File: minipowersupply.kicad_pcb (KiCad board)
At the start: 2 copper layers, 145.9 x 37.4 mm, 56 parts, among them J1 Conn_01x08_Female, J2 Conn_01x08_Female, J3 Conn_01x03_Female, J4 Conn_01x08_Female, J5 Conn_01x03_Female, J6 Conn_01x03_Female, J7 Conn_01x02_Female, J8 Conn_01x08_Female, J9 Conn_01x02_Female, Q1 BC817, U1 LM7805_TO220, U10 LM317L_TO92, U11 LM337L_TO92, U14 ACS70331EOLCTR-2P5U3, U2 ACS70331EOLCTR-2P5U3, U3 ACS70331EOLCTR-2P5U3, U4 ACS70331EOLCTR-2P5U3, U5 ACS70331EOLCTR-2P5U3, U9 CD74HC4067SM

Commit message: last TH mounting board
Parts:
- removed the R10 at (148.8, 70.3)
- removed R22, R23: R_Small, Resistor_THT:R_Axial_DIN0207_L6.3mm_D2.5mm_P5.08mm_Vertical
- removed the R9 at (92.0, 113.2)
- removed U14: ACS70331EOLCTR-2P5U3, ACS70331EOLCTR-2P5U3:SOIC127P600X175-8N
- added C39: C, Capacitor_THT:C_Disc_D8.0mm_W5.0mm_P5.00mm, F.Cu at (41.4, 107.2)
- added D7: DIODE, Diode_THT:D_T-1_P10.16mm_Horizontal, F.Cu at (158.6, 43.3)
- added D8: DIODE, Diode_THT:D_T-1_P10.16mm_Horizontal, F.Cu at (148.5, 40.1)
- added D9: DIODE, Diode_THT:D_T-1_P10.16mm_Horizontal, F.Cu at (59.8, 137.4)
- added J1: Conn_01x01_Female, Connector_PinHeader_2.54mm:PinHeader_1x01_P2.54mm_Vertical, F.Cu at (99.3, 116.3)
- added J2: Conn_01x03_Male, Connector_PinHeader_2.54mm:PinHeader_1x03_P2.54mm_Horizontal, F.Cu at (106.5, 92.5)
- added J3: Conn_01x01_Female, Connector_PinHeader_2.54mm:PinHeader_1x01_P2.54mm_Vertical, F.Cu at (107.7, 116.3)
- added J4: Conn_01x01_Female, Connector_PinHeader_2.54mm:PinHeader_1x01_P2.54mm_Vertical, F.Cu at (136.1, 116.3)
- added J5: Conn_01x03_Male, Connector_PinHeader_2.54mm:PinHeader_1x03_P2.54mm_Horizontal, B.Cu at (131.3, 92.5)
- added J6: Conn_01x01_Female, Connector_PinHeader_2.54mm:PinHeader_1x01_P2.54mm_Vertical, F.Cu at (125.0, 116.3)
- added J7: Conn_01x01_Female, Connector_PinHeader_2.54mm:PinHeader_1x01_P2.54mm_Vertical, F.Cu at (118.4, 116.3)
- added J8: Conn_01x03_Male, Connector_PinHeader_2.54mm:PinHeader_1x03_P2.54mm_Horizontal, B.Cu at (121.4, 92.5)
- added J9: Conn_01x01_Female, Connector_PinHeader_2.54mm:PinHeader_1x01_P2.54mm_Vertical, F.Cu at (112.8, 116.3)
- added R1: R_Small, Resistor_THT:R_Axial_DIN0207_L6.3mm_D2.5mm_P5.08mm_Vertical, F.Cu at (105.9, 107.4)
- added R14: R, Resistor_THT:R_Axial_DIN0207_L6.3mm_D2.5mm_P5.08mm_Vertical, F.Cu at (91.3, 104.4)
- added R15: R, Resistor_THT:R_Axial_DIN0207_L6.3mm_D2.5mm_P5.08mm_Vertical, F.Cu at (86.6, 101.2)
- added R16: R_Small, Resistor_THT:R_Axial_DIN0207_L6.3mm_D2.5mm_P5.08mm_Vertical, F.Cu at (97.3, 107.4)
- added R17: R_Small, Resistor_THT:R_Axial_DIN0207_L6.3mm_D2.5mm_P5.08mm_Vertical, F.Cu at (102.0, 110.6)
- added R18: R, Resistor_THT:R_Axial_DIN0207_L6.3mm_D2.5mm_P5.08mm_Vertical, F.Cu at (76.8, 137.0)
- added R19: R, Resistor_THT:R_Axial_DIN0207_L6.3mm_D2.5mm_P5.08mm_Vertical, F.Cu at (86.4, 120.8)
- added R2: R_Small, Resistor_THT:R_Axial_DIN0207_L6.3mm_D2.5mm_P5.08mm_Vertical, F.Cu at (110.5, 110.7)
- added R20: R, Resistor_THT:R_Axial_DIN0207_L6.3mm_D2.5mm_P5.08mm_Vertical, F.Cu at (86.4, 116.8)
- added U1: ACS70331EOLCTR-2P5U3, ACS70331EOLCTR-2P5U3:SOIC127P600X175-8N, F.Cu at (107.5, 101.8)
- added U10: ACS70331EOLCTR-2P5U3, ACS70331EOLCTR-2P5U3:SOIC127P600X175-8N, F.Cu at (99.1, 101.8)
- Q1: moved to F.Cu
- R11: value R_Small -> 698
- R3: value 698 -> R_Small
- U4: value ACS70331EOLCTR-2P5U3 -> CD74HC4067SM; footprint ACS70331EOLCTR-2P5U3:SOIC127P600X175-8N -> Package_SO:SSOP-24_5.3x8.2mm_P0.65mm
- U6: renamed from U1; moved to B.Cu
- U9: value CD74HC4067SM -> Opamp_Dual; footprint Package_SO:SSOP-24_5.3x8.2mm_P0.65mm -> Package_TO_SOT_SMD:SOT-223-8
- moved R3 115.2 mm to (132.1, 107.4)
- moved C27 70.1 mm to (139.8, 50.8)
- moved R10 67.6 mm to (148.8, 47.4), turned to -90 degrees
- moved C29 65.9 mm to (157.5, 50.8), turned to 180 degrees
- moved U5 49.7 mm to (118.2, 102.1), turned to 180 degrees
- moved R4 48.2 mm to (136.7, 110.6), turned to 180 degrees
- moved U9 48.0 mm to (88.7, 111.2), turned to 180 degrees
- moved R5 43.8 mm to (123.7, 107.4)
- moved U2 43.0 mm to (134.7, 102.1), turned to 180 degrees
- moved U7 39.9 mm to (166.9, 43.1), turned to -90 degrees
- moved A1 39.8 mm to (60.0, 92.7)
- moved J17 37.9 mm to (168.0, 54.5)
- moved R8 37.7 mm to (119.7, 110.6), turned to 180 degrees
- moved J12 37.4 mm to (119.5, 59.6)
- moved J14 37.1 mm to (124.3, 59.6)
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- renumbered C1 to C23, C2 to C24, C3 to C27, C4 to C28, C5 to C29, C6 to C30, C7 to C31, C8 to C32, C9 to C33, J3 to J10, J1 to J11, J5 to J12, J2 to J13, J6 to J14, J4 to J15, J7 to J16, J8 to J17, J9 to J18, R2 to R10, R16 to R12, R17 to R13, R1 to R9, U10 to U7, U11 to U8
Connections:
- net Earth renamed /Unregulated Power/GND
- A1 pad 20: Net-(A1-Pad20) -> unconnected-(A1-Pad20)
- A1 pad 29: GNDREF -> / Measure and Mux/GND
- A1 pad 4: GNDREF -> / Measure and Mux/GND
- DS1 pad 1: unconnected-(DS1-Pad1) -> / Measure and Mux/GND
- DS1 pad 30: unconnected-(DS1-Pad1) -> / Measure and Mux/GND
- R11 pad 1: / Measure and Mux/Curent and Volt8/Vsense -> Net-(D7-Pad2)
- R11 pad 2: / Measure and Mux/Curent and Volt4/GND -> /Clock and TTL/GND_0
- R3 pad 1: Net-(D7-Pad2) -> / Measure and Mux/Curent and Volt6/Out V
- R3 pad 2: /Clock and TTL/GND_0 -> / Measure and Mux/Curent and Volt6/Vsense
- R4 pad 1: / Measure and Mux/Curent and Volt5/Out V -> / Measure and Mux/Curent and Volt6/Vsense
- R4 pad 2: / Measure and Mux/Curent and Volt5/Vsense -> / Measure and Mux/GND
- R5 pad 1: / Measure and Mux/Curent and Volt5/Vsense -> / Measure and Mux/Curent and Volt7/Out V
- R5 pad 2: / Measure and Mux/Curent and Volt4/GND -> / Measure and Mux/Curent and Volt7/Vsense
- R6 pad 1: / Measure and Mux/Curent and Volt6/Out V -> / Measure and Mux/Curent and Volt7/Vsense
- R6 pad 2: / Measure and Mux/Curent and Volt6/Vsense -> / Measure and Mux/GND
- R7 pad 1: / Measure and Mux/Curent and Volt6/Vsense -> / Measure and Mux/Curent and Volt8/Out V
- R7 pad 2: / Measure and Mux/Curent and Volt4/GND -> / Measure and Mux/Curent and Volt8/Vsense
- R8 pad 1: / Measure and Mux/Curent and Volt7/Out V -> / Measure and Mux/Curent and Volt8/Vsense
- R8 pad 2: / Measure and Mux/Curent and Volt7/Vsense -> / Measure and Mux/GND
- U2 pad 1: / Measure and Mux/Curent and Volt5/Out V -> / Measure and Mux/Curent and Volt6/Out V
- U2 pad 2: / Measure and Mux/Curent and Volt5/Out V -> / Measure and Mux/Curent and Volt6/Out V
- U2 pad 3: / Measure and Mux/Vunreg- -> / Measure and Mux/Curent and Volt6/Vin
- U2 pad 4: / Measure and Mux/Vunreg- -> / Measure and Mux/Curent and Volt6/Vin
- U2 pad 5: / Measure and Mux/Curent and Volt4/GND -> / Measure and Mux/GND
- U2 pad 7: / Measure and Mux/Curent and Volt5/Isense -> / Measure and Mux/Curent and Volt6/Isense
- U3 pad 1: / Measure and Mux/Curent and Volt6/Out V -> / Measure and Mux/Curent and Volt7/Out V
- U3 pad 2: / Measure and Mux/Curent and Volt6/Out V -> / Measure and Mux/Curent and Volt7/Out V
- U3 pad 3: / Measure and Mux/Curent and Volt6/Vin -> / Measure and Mux/Curent and Volt7/Vin
- U3 pad 4: / Measure and Mux/Curent and Volt6/Vin -> / Measure and Mux/Curent and Volt7/Vin
- U3 pad 5: / Measure and Mux/Curent and Volt4/GND -> / Measure and Mux/GND
- U3 pad 7: / Measure and Mux/Curent and Volt6/Isense -> / Measure and Mux/Curent and Volt7/Isense
- U4 pad 1: / Measure and Mux/Curent and Volt7/Out V -> / Measure and Mux/Aout
- U4 pad 2: / Measure and Mux/Curent and Volt7/Out V -> / Measure and Mux/Curent and Volt7/Isense
- U4 pad 3: / Measure and Mux/Curent and Volt7/Vin -> / Measure and Mux/Unity Inverter1/Ainv
- U4 pad 4: / Measure and Mux/Curent and Volt7/Vin -> / Measure and Mux/Curent and Volt6/Isense
- U4 pad 5: / Measure and Mux/Curent and Volt4/GND -> / Measure and Mux/Curent and Volt6/Vsense
- U4 pad 6: unconnected-(U4-Pad6) -> / Measure and Mux/Curent and Volt5/Isense
- U4 pad 7: / Measure and Mux/Curent and Volt7/Isense -> / Measure and Mux/Unity Inverter/Ainv
- U4 pad 8: / Measure and Mux/3v3 -> / Measure and Mux/Curent and Volt4/Isense
- U5 pad 5: / Measure and Mux/Curent and Volt4/GND -> / Measure and Mux/GND
- U9 pad 1: / Measure and Mux/Aout -> / Measure and Mux/Unity Inverter/Ainv
- U9 pad 2: / Measure and Mux/Curent and Volt7/Isense -> / Measure and Mux/Curent and Volt5/Vsense
- U9 pad 3: / Measure and Mux/Curent and Volt7/Vsense -> Net-(R19-Pad1)
- U9 pad 4: / Measure and Mux/Curent and Volt6/Isense -> / Measure and Mux/Vunreg-
- U9 pad 5: / Measure and Mux/Curent and Volt6/Vsense -> Net-(R14-Pad1)
- U9 pad 6: / Measure and Mux/Curent and Volt5/Isense -> / Measure and Mux/Curent and Volt7/Vsense
- U9 pad 7: / Measure and Mux/Curent and Volt5/Vsense -> / Measure and Mux/Unity Inverter1/Ainv
- U9 pad 8: / Measure and Mux/Curent and Volt4/Isense -> / Measure and Mux/Vunreg+
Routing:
- net (no net): track 36.7 -> 0.00 mm
- net Net-(J16-Pad2): track 0.00 -> 17.5 mm
- net /Clock and TTL/CK: track 42.1 -> 25.6 mm, vias 1 -> 0
- net Net-(C32-Pad1): track 8.62 -> 24.9 mm
- net /Unregulated Power/V-: track 40.5 -> 49.3 mm
- net Net-(J18-Pad2): track 0.00 -> 7.56 mm
- net Net-(C33-Pad2): track 23.3 -> 30.6 mm
- net /Unregulated Power/V+: track 69.1 -> 62.2 mm
- net Net-(C31-Pad1): track 27.8 -> 34.1 mm
- net Net-(C25-Pad2): track 12.2 -> 18.2 mm
- net Net-(C22-Pad1): track 12.7 -> 18.7 mm
- net Net-(C26-Pad1): track 7.46 -> 13.4 mm
- net Net-(J11-Pad8): track 7.29 -> 12.9 mm
- net /Clock and TTL/GND_0: track 0.00 -> 3.80 mm, vias 0 -> 1
- net Net-(C27-Pad1): track 11.7 -> 9.09 mm
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- added copper zone on B.Cu, net /DualAdj/GND
- added copper zone on F.Cu, net /DualAdj/GND
- removed copper zone on B.Cu, net (none)
- removed copper zone on F.Cu, net (none)
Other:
- board size 145.9 x 37.4 mm -> 149.9 x 37.3 mm

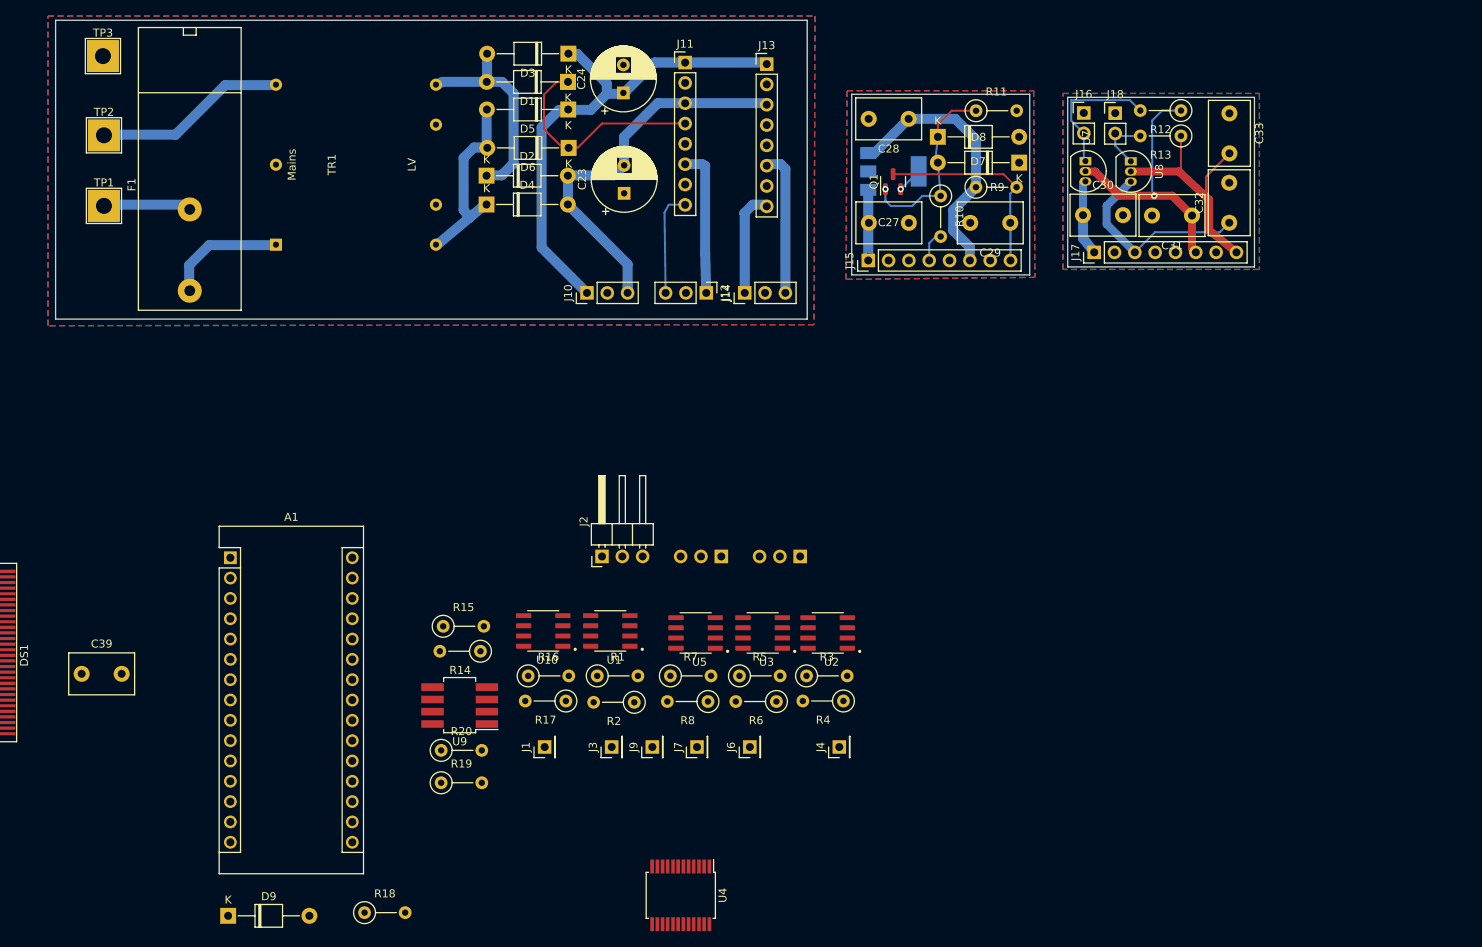
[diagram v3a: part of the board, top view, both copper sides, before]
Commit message: all SMD components going into boards
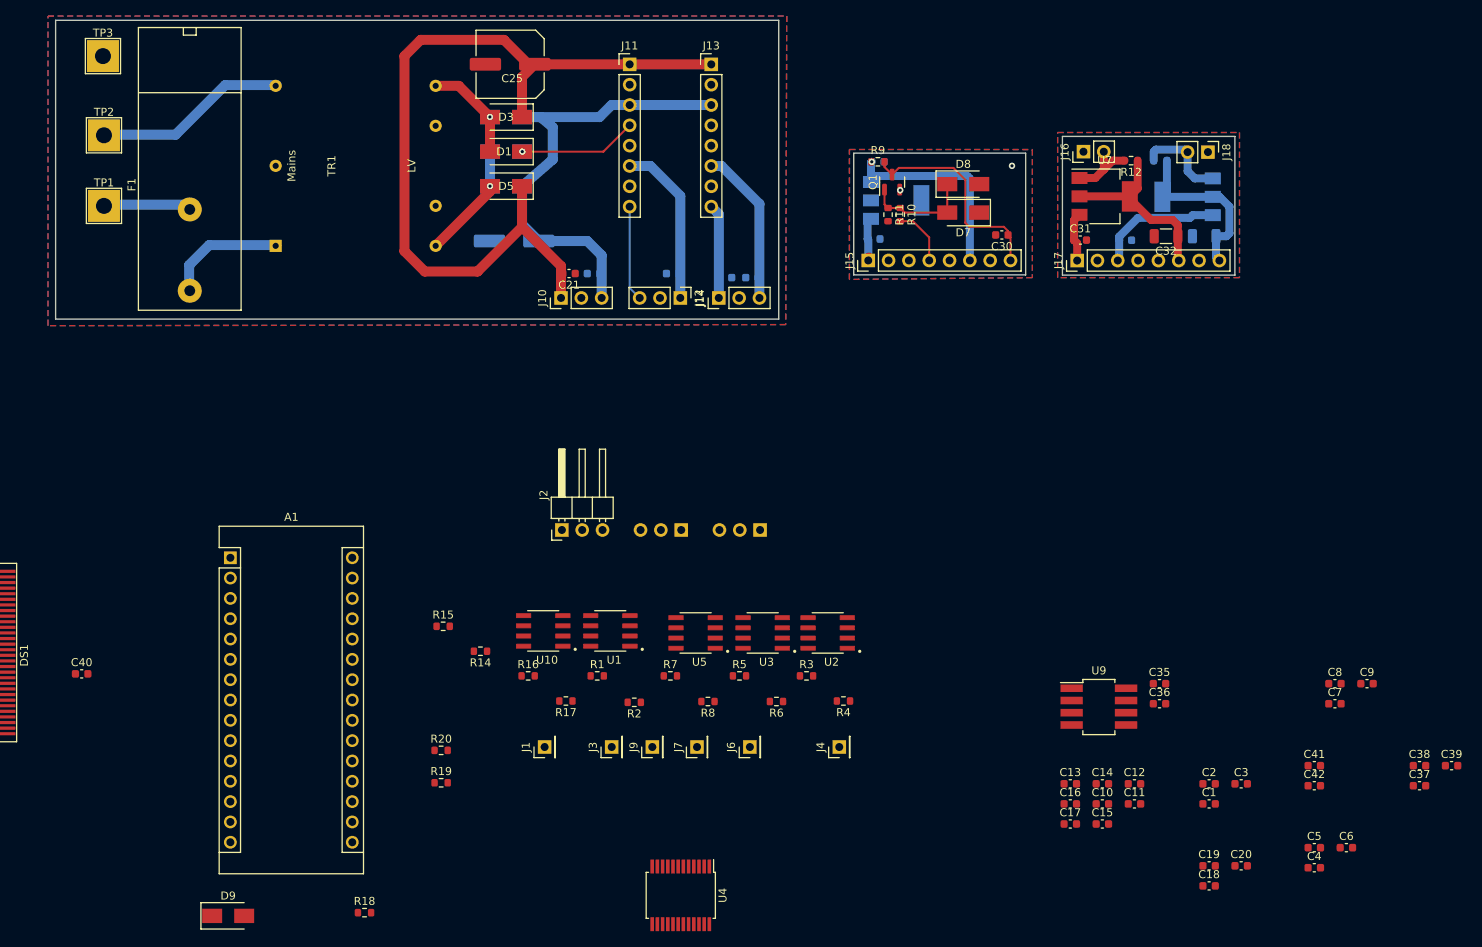
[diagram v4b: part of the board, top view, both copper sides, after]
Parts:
- added C1: 0.1uF, Capacitor_SMD:C_0603_1608Metric, F.Cu at (182.4, 123.4)
- added C10: 0.1uF, Capacitor_SMD:C_0603_1608Metric, F.Cu at (169.0, 123.4)
- added C11: 0.1uF, Capacitor_SMD:C_0603_1608Metric, F.Cu at (173.0, 123.4)
- added C12: 0.1uF, Capacitor_SMD:C_0603_1608Metric, F.Cu at (173.0, 120.9)
- added C13: 0.1uF, Capacitor_SMD:C_0603_1608Metric, F.Cu at (165.0, 120.9)
- added C14: 0.1uF, Capacitor_SMD:C_0603_1608Metric, F.Cu at (169.0, 120.9)
- added C15: 0.1uF, Capacitor_SMD:C_0603_1608Metric, F.Cu at (169.0, 126.0)
- added C16: 0.1uF, Capacitor_SMD:C_0603_1608Metric, F.Cu at (165.0, 123.4)
- added C17: 0.1uF, Capacitor_SMD:C_0603_1608Metric, F.Cu at (165.0, 126.0)
- added C18: 0.1uF, Capacitor_SMD:C_0603_1608Metric, F.Cu at (182.4, 133.7)
- added C19: 0.1uF, Capacitor_SMD:C_0603_1608Metric, F.Cu at (182.4, 131.2)
- added C2: 0.1uF, Capacitor_SMD:C_0603_1608Metric, F.Cu at (182.4, 120.9)
- added C20: 0.1uF, Capacitor_SMD:C_0603_1608Metric, F.Cu at (186.4, 131.2)
- added C21: 0.1uF, Capacitor_SMD:C_0603_1608Metric, F.Cu at (102.4, 57.1)
- added C22: 0.1uF, Capacitor_SMD:C_0603_1608Metric, B.Cu at (105.4, 57.1)
- added C23: 0.1uF, Capacitor_SMD:C_0603_1608Metric, B.Cu at (115.3, 57.1)
- added C26: 0.1uF, Capacitor_SMD:C_0603_1608Metric, B.Cu at (125.2, 57.7)
- added C27: 0.1uF, Capacitor_SMD:C_0603_1608Metric, B.Cu at (121.9, 57.7)
- added C3: 0.1uF, Capacitor_SMD:C_0603_1608Metric, F.Cu at (186.4, 120.9)
- added C35: 0.1uF, Capacitor_SMD:C_0603_1608Metric, F.Cu at (176.2, 108.4)
- added C36: 0.1uF, Capacitor_SMD:C_0603_1608Metric, F.Cu at (176.2, 110.9)
- added C37: 0.1uF, Capacitor_SMD:C_0603_1608Metric, F.Cu at (208.7, 121.2)
- added C38: 0.1uF, Capacitor_SMD:C_0603_1608Metric, F.Cu at (208.7, 118.7)
- added C39: 0.1uF, Capacitor_SMD:C_0603_1608Metric, F.Cu at (212.7, 118.7)
- added C4: 0.1uF, Capacitor_SMD:C_0603_1608Metric, F.Cu at (195.5, 131.4)
- added C41: 0.1uF, Capacitor_SMD:C_0603_1608Metric, F.Cu at (195.5, 118.7)
- added C42: 0.1uF, Capacitor_SMD:C_0603_1608Metric, F.Cu at (195.5, 121.2)
- added C5: 0.1uF, Capacitor_SMD:C_0603_1608Metric, F.Cu at (195.5, 128.9)
- added C6: 0.1uF, Capacitor_SMD:C_0603_1608Metric, F.Cu at (199.5, 128.9)
- added C7: 0.1uF, Capacitor_SMD:C_0603_1608Metric, F.Cu at (198.1, 110.9)
- added C8: 0.1uF, Capacitor_SMD:C_0603_1608Metric, F.Cu at (198.1, 108.4)
- added C9: 0.1uF, Capacitor_SMD:C_0603_1608Metric, F.Cu at (202.1, 108.4)
- C24: renamed from C23; footprint Capacitor_THT:CP_Radial_D8.0mm_P3.50mm -> Capacitor_SMD:C_Elec_8x6.2; moved to B.Cu
- C25: renamed from C24; footprint Capacitor_THT:CP_Radial_D8.0mm_P3.50mm -> Capacitor_SMD:C_Elec_8x6.2
- C28: renamed from C27; value 100nF -> 0.1uF; footprint Capacitor_THT:C_Disc_D8.0mm_W5.0mm_P5.00mm -> Capacitor_SMD:C_0603_1608Metric; moved to B.Cu
- C29: renamed from C28; value 100nF -> 0.1uF; footprint Capacitor_THT:C_Disc_D8.0mm_W5.0mm_P5.00mm -> Capacitor_SMD:C_0603_1608Metric; moved to B.Cu
- C30: renamed from C29; value 100nF -> 0.1uF; footprint Capacitor_THT:C_Disc_D8.0mm_W5.0mm_P5.00mm -> Capacitor_SMD:C_0603_1608Metric
- C31: renamed from C30; value 100nF -> 0.1uF; footprint Capacitor_THT:C_Disc_D8.0mm_W5.0mm_P5.00mm -> Capacitor_SMD:C_0603_1608Metric
- C32: renamed from C31; footprint Capacitor_THT:C_Disc_D8.0mm_W5.0mm_P5.00mm -> Capacitor_SMD:C_1206_3216Metric
- C33: renamed from C32; value 100nF -> 0.1uF; footprint Capacitor_THT:C_Disc_D8.0mm_W5.0mm_P5.00mm -> Capacitor_SMD:C_0603_1608Metric; moved to B.Cu
- C34: renamed from C33; footprint Capacitor_THT:C_Disc_D8.0mm_W5.0mm_P5.00mm -> Capacitor_SMD:C_1206_3216Metric; moved to B.Cu
- C40: renamed from C39; value C -> 0.1uF; footprint Capacitor_THT:C_Disc_D8.0mm_W5.0mm_P5.00mm -> Capacitor_SMD:C_0603_1608Metric
- D1, D3, D5: value D -> S1K-13-F; footprint Diode_THT:D_T-1_P10.16mm_Horizontal -> Diode_SMD:D_SMA
- D2, D4, D6: value D -> S1K-13-F; footprint Diode_THT:D_T-1_P10.16mm_Horizontal -> Diode_SMD:D_SMA; moved to B.Cu
- D7, D8, D9: value DIODE -> S1K-13-F; footprint Diode_THT:D_T-1_P10.16mm_Horizontal -> Diode_SMD:D_SMA
- R1, R16, R3, R5, R7: value R_Small -> 20k; footprint Resistor_THT:R_Axial_DIN0207_L6.3mm_D2.5mm_P5.08mm_Vertical -> Resistor_SMD:R_0603_1608Metric
- R10, R11, R12, R9: footprint Resistor_THT:R_Axial_DIN0207_L6.3mm_D2.5mm_P5.08mm_Vertical -> Resistor_SMD:R_0603_1608Metric
- R13: footprint Resistor_THT:R_Axial_DIN0207_L6.3mm_D2.5mm_P5.08mm_Vertical -> Resistor_SMD:R_0603_1608Metric; moved to B.Cu
- R14, R15, R18, R19, R20: value R -> 10k; footprint Resistor_THT:R_Axial_DIN0207_L6.3mm_D2.5mm_P5.08mm_Vertical -> Resistor_SMD:R_0603_1608Metric
- R17, R2, R4, R6, R8: value R_Small -> 10k; footprint Resistor_THT:R_Axial_DIN0207_L6.3mm_D2.5mm_P5.08mm_Vertical -> Resistor_SMD:R_0603_1608Metric
- U7: footprint Package_TO_SOT_THT:TO-92_Inline -> Package_TO_SOT_SMD:SOT-223-3_TabPin2
- U8: footprint Package_TO_SOT_THT:TO-92_Inline -> Package_TO_SOT_SMD:SOT-223-3_TabPin2; moved to B.Cu
- U9: value Opamp_Dual -> LM358
- moved U9 79.9 mm to (168.6, 111.3), turned to 0 degrees
- moved R11 17.0 mm to (142.2, 49.8), turned to -90 degrees
- moved C34 15.7 mm to (181.8, 52.5), turned to 0 degrees
- moved C24 15.0 mm to (95.5, 53.1), turned to 0 degrees
- moved C25 14.6 mm to (95.0, 31.0), turned to 180 degrees
- moved C33 13.2 mm to (171.9, 53.0), turned to 0 degrees
- moved R9 12.7 mm to (141.0, 43.2)
- moved J18 12.6 mm to (182.2, 42.0), turned to -90 degrees
- moved D5 12.3 mm to (94.5, 46.2)
- moved D1 11.7 mm to (94.5, 41.9)
- moved D3 11.1 mm to (94.5, 37.6)
- moved D7 9.37 mm to (151.6, 49.5)
- moved R12 8.83 mm to (172.6, 43.0)
- moved U8 8.36 mm to (179.7, 47.6), turned to 180 degrees
- moved D6 7.84 mm to (94.5, 41.9)
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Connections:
- R15 pad 1: / Measure and Mux/GND -> / Measure and Mux/Curent and Volt7/Vsense
- R20 pad 1: / Measure and Mux/GND -> / Measure and Mux/Curent and Volt5/Vsense
- U9 pad 2: / Measure and Mux/Curent and Volt5/Vsense -> / Measure and Mux/GND
- U9 pad 4: / Measure and Mux/Vunreg- -> / Measure and Mux/Vunreg+
- U9 pad 6: / Measure and Mux/Curent and Volt7/Vsense -> / Measure and Mux/GND
- U9 pad 8: / Measure and Mux/Vunreg+ -> / Measure and Mux/Vunreg-
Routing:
- net /Unregulated Power/V+: track 62.2 -> 108.5 mm
- net Net-(D1-Pad2): track 26.5 -> 12.7 mm, vias 0 -> 1
- net Net-(D1-Pad1): track 27.6 -> 14.8 mm, vias 0 -> 1
- net Net-(C32-Pad1): track 34.1 -> 23.3 mm, vias 1 -> 0
- net Net-(D7-Pad2): track 24.2 -> 13.7 mm, vias 1 -> 0
- net Net-(D4-Pad1): track 24.0 -> 14.6 mm, vias 0 -> 1
- net Net-(C33-Pad1): track 24.9 -> 15.9 mm
- net Net-(J16-Pad2): track 17.5 -> 8.76 mm
- net Net-(C34-Pad2): track 30.6 -> 22.0 mm
- net /Unregulated Power/V-: track 49.3 -> 57.8 mm
- net +5VA: track 33.5 -> 25.6 mm, vias 0 -> 1
- net Net-(J18-Pad2): track 7.56 -> 11.5 mm
- net /Clock and TTL/GND_0: track 3.80 -> 0.00 mm, vias 1 -> 2
- net Net-(C28-Pad1): track 9.09 -> 5.46 mm
- net Net-(J15-Pad4): track 3.94 -> 7.33 mm
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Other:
- board size 149.9 x 37.3 mm -> 147.4 x 37.3 mm
